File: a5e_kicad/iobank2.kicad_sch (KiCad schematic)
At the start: 2 parts, among them U1 A5EB013B-B23B

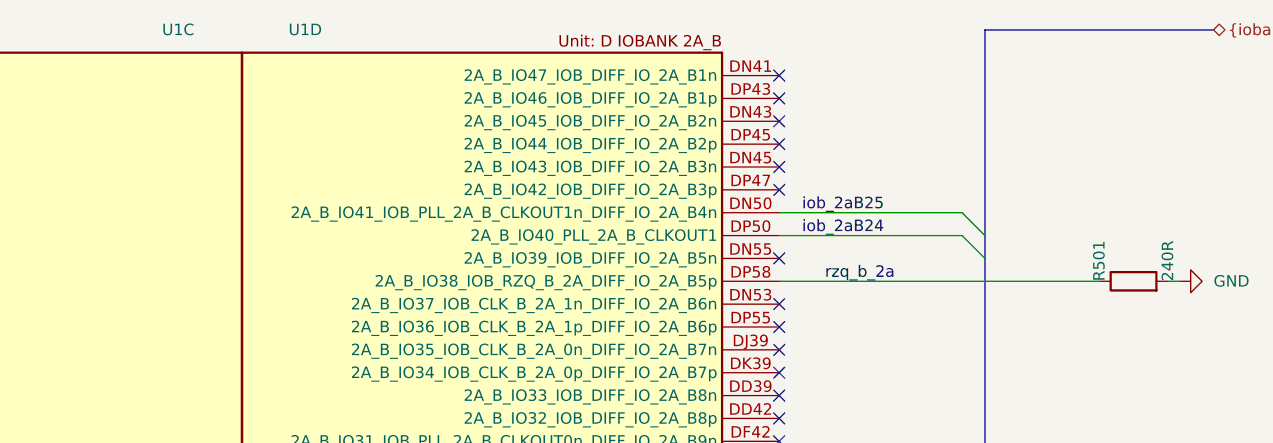
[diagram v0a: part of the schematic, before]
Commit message: add vias to lppdr balls
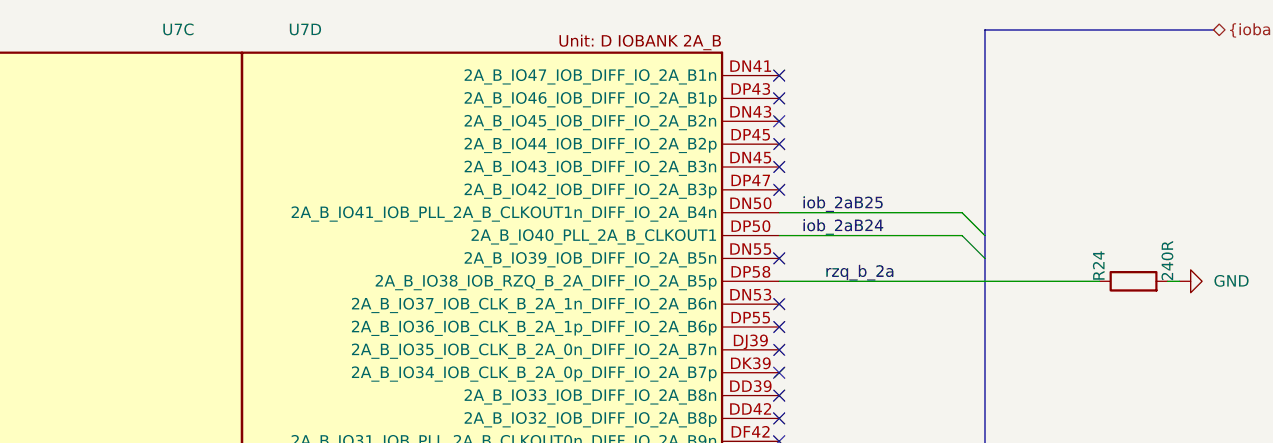
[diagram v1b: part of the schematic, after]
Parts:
- renumbered R501 to R24, U1 to U7
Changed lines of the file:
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@@
 		(in_pos_files yes)
 		(dnp no)
-		(property "Reference" "U1"
+		(property "Reference" "U7"
 			(at 144.78 22.86 0)
 			(show_name no)
@@
 			(project "agilex_3_soc"
 				(path "/a5b98d95-6877-4284-904f-d04e32723ae0/75d90890-a51c-4e7c-a03e-f25381d85068"
-					(reference "U1")
+					(reference "U7")
 					(unit 4)
 				)
@@
 		(in_pos_files yes)
 		(dnp no)
-		(property "Reference" "#PWR0501"
+		(property "Reference" "#PWR050"
 			(at 246.38 50.8 0)
 			(hide yes)
@@
 			(project "agilex_3_soc"
 				(path "/a5b98d95-6877-4284-904f-d04e32723ae0/75d90890-a51c-4e7c-a03e-f25381d85068"
-					(reference "#PWR0501")
+					(reference "#PWR050")
 					(unit 1)
 				)
@@
 		(in_pos_files yes)
 		(dnp no)
-		(property "Reference" "U1"
+		(property "Reference" "U7"
 			(at 127 22.86 0)
 			(show_name no)
@@
 			(project "agilex_3_soc"
 				(path "/a5b98d95-6877-4284-904f-d04e32723ae0/75d90890-a51c-4e7c-a03e-f25381d85068"
-					(reference "U1")
+					(reference "U7")
 					(unit 3)
 				)
@@
 		(in_pos_files yes)
 		(dnp no)
-		(property "Reference" "R501"
+		(property "Reference" "R24"
 			(at 231.14 50.8 0)
 			(show_name no)
@@
 			(project "agilex_3_soc"
 				(path "/a5b98d95-6877-4284-904f-d04e32723ae0/75d90890-a51c-4e7c-a03e-f25381d85068"
-					(reference "R501")
+					(reference "R24")
 					(unit 1)
 				)
